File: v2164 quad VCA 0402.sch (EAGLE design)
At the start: 43 parts, among them IC1 TL072JD, IC2 TL072JD

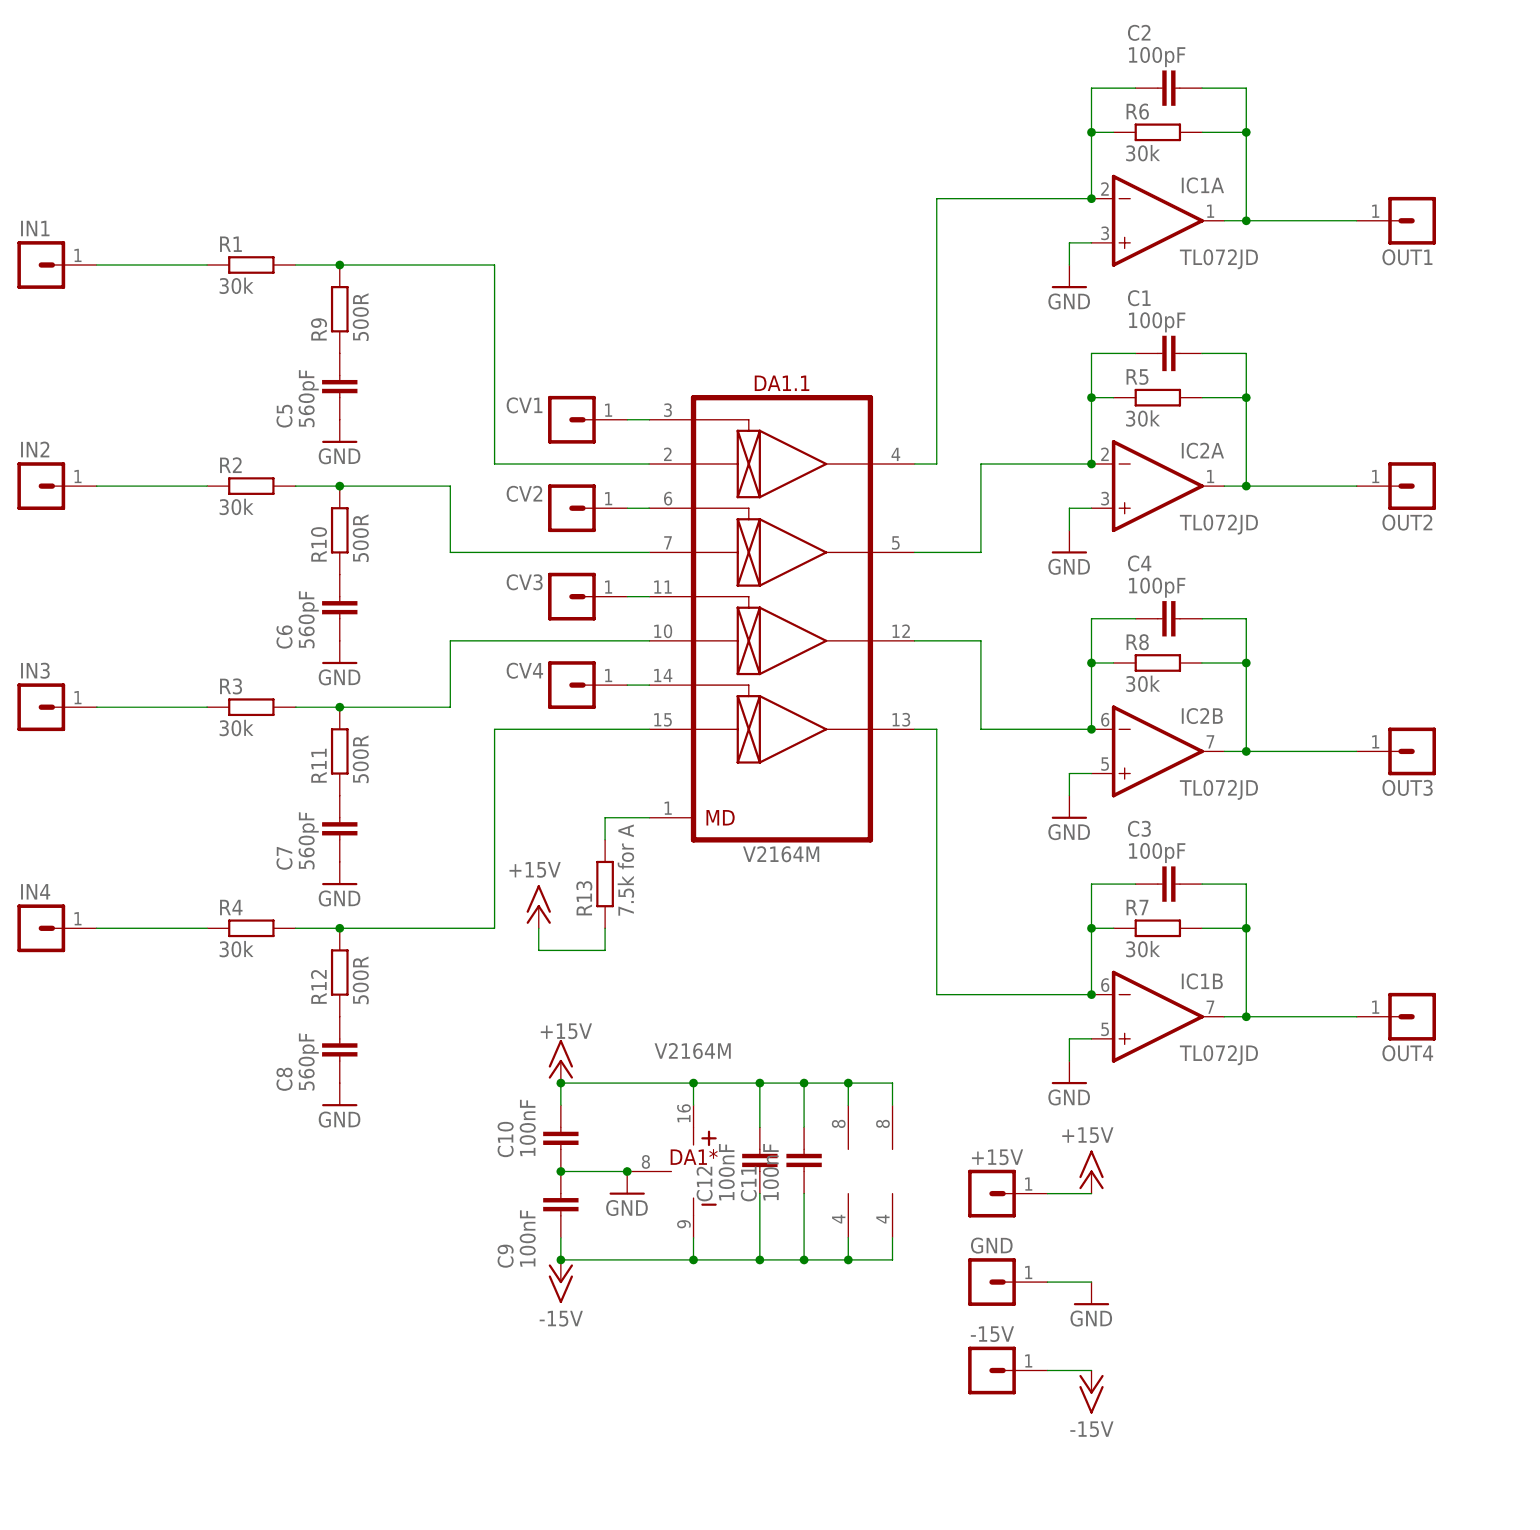
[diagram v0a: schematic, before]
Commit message: Finished top layer on both boards i think
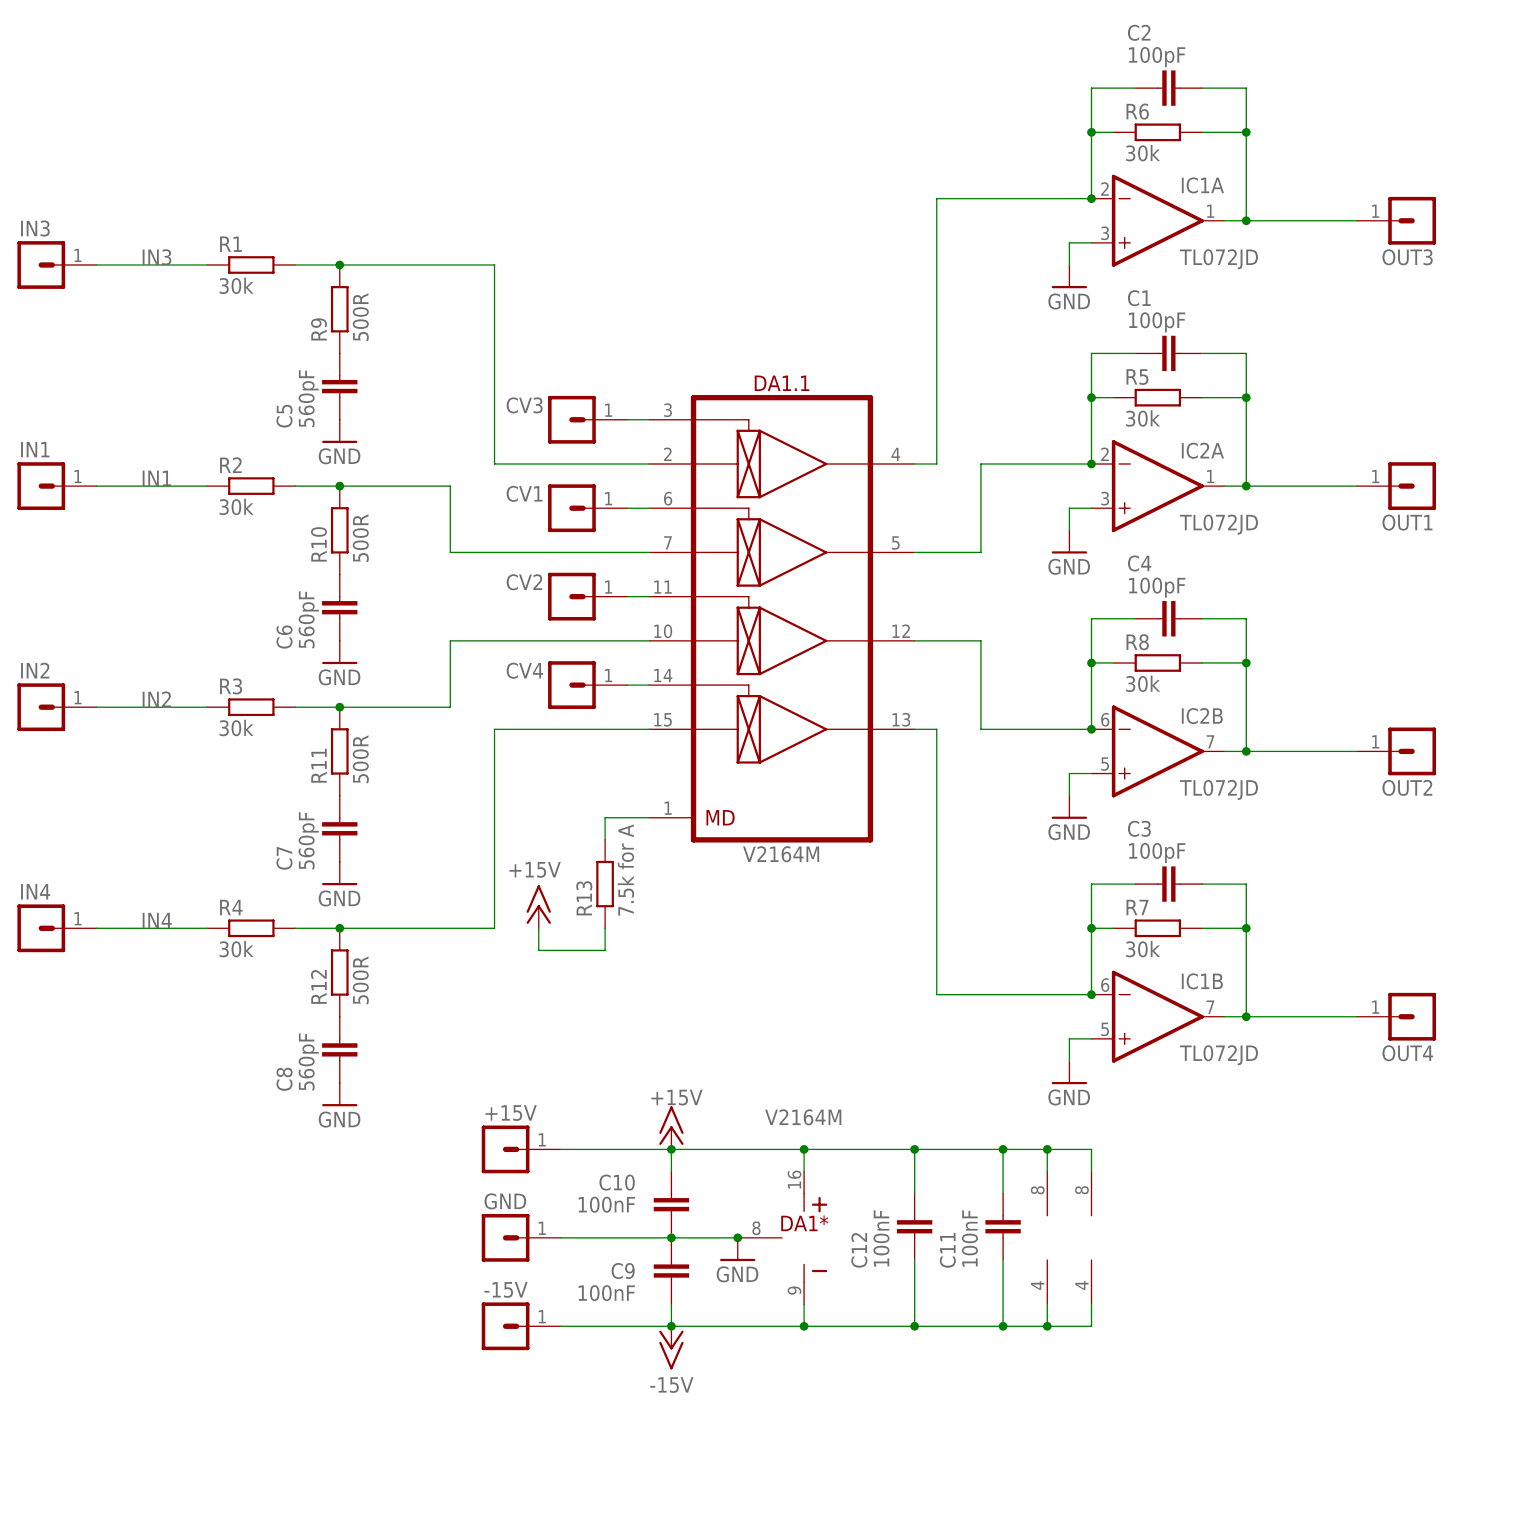
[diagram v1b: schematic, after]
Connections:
- net CV1: now also DA1.1.CV2; no longer DA1.1.CV1
- net CV2: now also DA1.1.CV3; no longer DA1.1.CV2
- net CV3: now also DA1.1.CV1; no longer DA1.1.CV3
- net IN1: now also R2.1; no longer R1.1
- net IN2: now also R3.1; no longer R2.1
- net IN3: now also R1.1; no longer R3.1
- net OUT1: now also C1.2, IC2A.OUT, R5.2; no longer C2.2, IC1A.OUT, R6.2
- net OUT2: now also C4.2, IC2B.OUT, R8.2; no longer C1.2, IC2A.OUT, R5.2
- net OUT3: now also C2.2, IC1A.OUT, R6.2; no longer C4.2, IC2B.OUT, R8.2
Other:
- moved on the sheet: +15V, -15V, C10, C11, C12, C9, CV1, CV2, CV3, DA1*, GND, IN1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

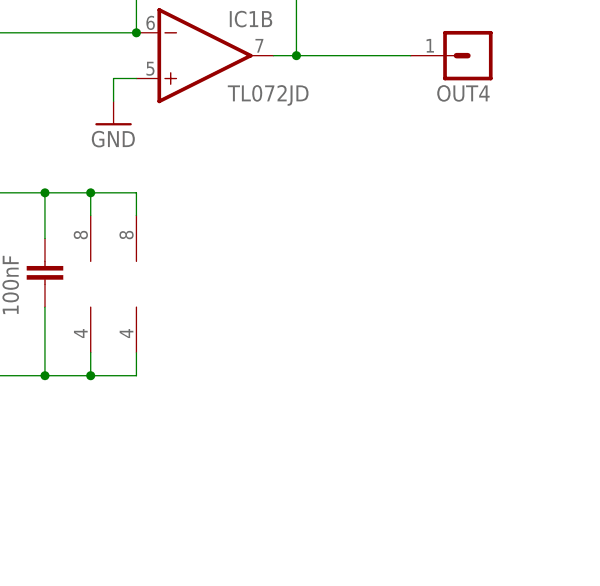
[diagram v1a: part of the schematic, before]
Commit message: Added optional shottky diodes
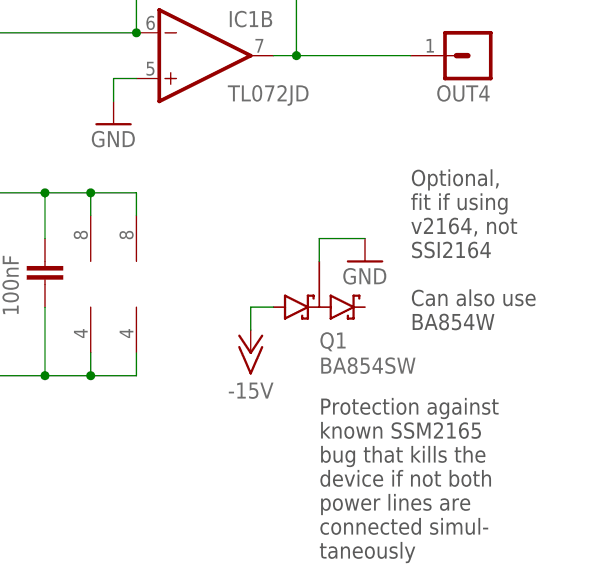
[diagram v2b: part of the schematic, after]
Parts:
- added Q1: BA854SW, joakim:BA854SW
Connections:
- net -15V: now also Q1.A1
- net GND: now also Q1.K1A2
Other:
- note added: "Optional, fit if using v2164, not SSI2164 Can also use BA854W"
- note added: "Protection against known SSM2165 bug that kills the device if not both power lines are connected simul- taneously"
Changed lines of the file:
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@@
 <part name="IC2" library="joakim" deviceset="TL072J" device="D"/>
 <part name="C12" library="rcl" library_urn="urn:adsk.eagle:library:334" deviceset="C-EU" device="C0402" package3d_urn="urn:adsk.eagle:package:23626/2" value="100nF"/>
+<part name="Q1" library="joakim" deviceset="BA854SW" device=""/>
+<part name="GND9" library="supply1" library_urn="urn:adsk.eagle:library:371" deviceset="GND" device=""/>
+<part name="P-1" library="supply1" library_urn="urn:adsk.eagle:library:371" deviceset="-15V" device=""/>
 </parts>
 <sheets>
 <sheet>
 <plain>
+<text x="127" y="-22.86" size="1.778" layer="97">Optional,
+fit if using
+v2164, not
+SSI2164
+Can also use
+BA854W</text>
+<text x="116.84" y="-48.26" size="1.778" layer="97">Protection against
+known SSM2165
+bug that kills the
+device if not both
+power lines are
+connected simul-
+taneously</text>
 </plain>
 <instances>
@@
 <attribute name="NAME" x="70.739" y="-21.336" size="1.778" layer="95" rot="R90"/>
 <attribute name="VALUE" x="73.279" y="-21.336" size="1.778" layer="96" rot="R90"/>
+</instance>
+<instance part="Q1" gate="G$1" x="114.3" y="-20.32" smashed="yes">
+<attribute name="NAME" x="116.84" y="-24.9174" size="1.778" layer="95"/>
+<attribute name="VALUE" x="116.84" y="-27.7114" size="1.778" layer="96"/>
+</instance>
+<instance part="GND9" gate="1" x="121.92" y="-15.24" smashed="yes">
+<attribute name="VALUE" x="119.38" y="-17.78" size="1.778" layer="96"/>
+</instance>
+<instance part="P-1" gate="1" x="109.22" y="-25.4" smashed="yes">
+<attribute name="VALUE" x="106.68" y="-30.48" size="1.778" layer="96"/>
 </instance>
 </instances>
@@
 <junction x="48.26" y="-17.78"/>
 <wire x1="35.56" y1="-17.78" x2="48.26" y2="-17.78" width="0.1524" layer="91"/>
+</segment>
+<segment>
+<pinref part="Q1" gate="G$1" pin="K1A2"/>
+<wire x1="116.84" y1="-15.24" x2="116.84" y2="-12.7" width="0.1524" layer="91"/>
+<pinref part="GND9" gate="1" pin="GND"/>
+<wire x1="116.84" y1="-12.7" x2="121.92" y2="-12.7" width="0.1524" layer="91"/>
 </segment>
 </net>
@@
 <wire x1="48.26" y1="-27.94" x2="35.56" y2="-27.94" width="0.1524" layer="91"/>
 </segment>
+<segment>
+<pinref part="P-1" gate="1" pin="-15V"/>
+<wire x1="109.22" y1="-22.86" x2="109.22" y2="-20.32" width="0.1524" layer="91"/>
+<pinref part="Q1" gate="G$1" pin="A1"/>
+<wire x1="109.22" y1="-20.32" x2="111.76" y2="-20.32" width="0.1524" layer="91"/>
+</segment>
 </net>
 <net name="OUT4" class="0">
@@
 </drawing>
 <compatibility>
+<note version="6.3" minversion="6.2.2" severity="warning">
+Since Version 6.2.2 text objects can contain more than one line,
+which will not be processed correctly with this version.
+</note>
 <note version="8.2" severity="warning">
 Since Version 8.2, EAGLE supports online libraries. The ids
